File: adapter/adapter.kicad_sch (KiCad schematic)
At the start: 32 parts, among them J1 Serial, J10 Ribbon, J11 Ribbon, J12 Ribbon, J13 serial, J14 serial, J2 Serial, J3 battery charge, J4 RGB, J5 RGB, J6 battery charge, J7 trackball, J8 trackball, J9 Ribbon, SW1 SW_SPST, SW2 SW_SPST, SW3 SW_SPDT, SW4 SW_SPDT, U1 eliteC, U2 eliteC

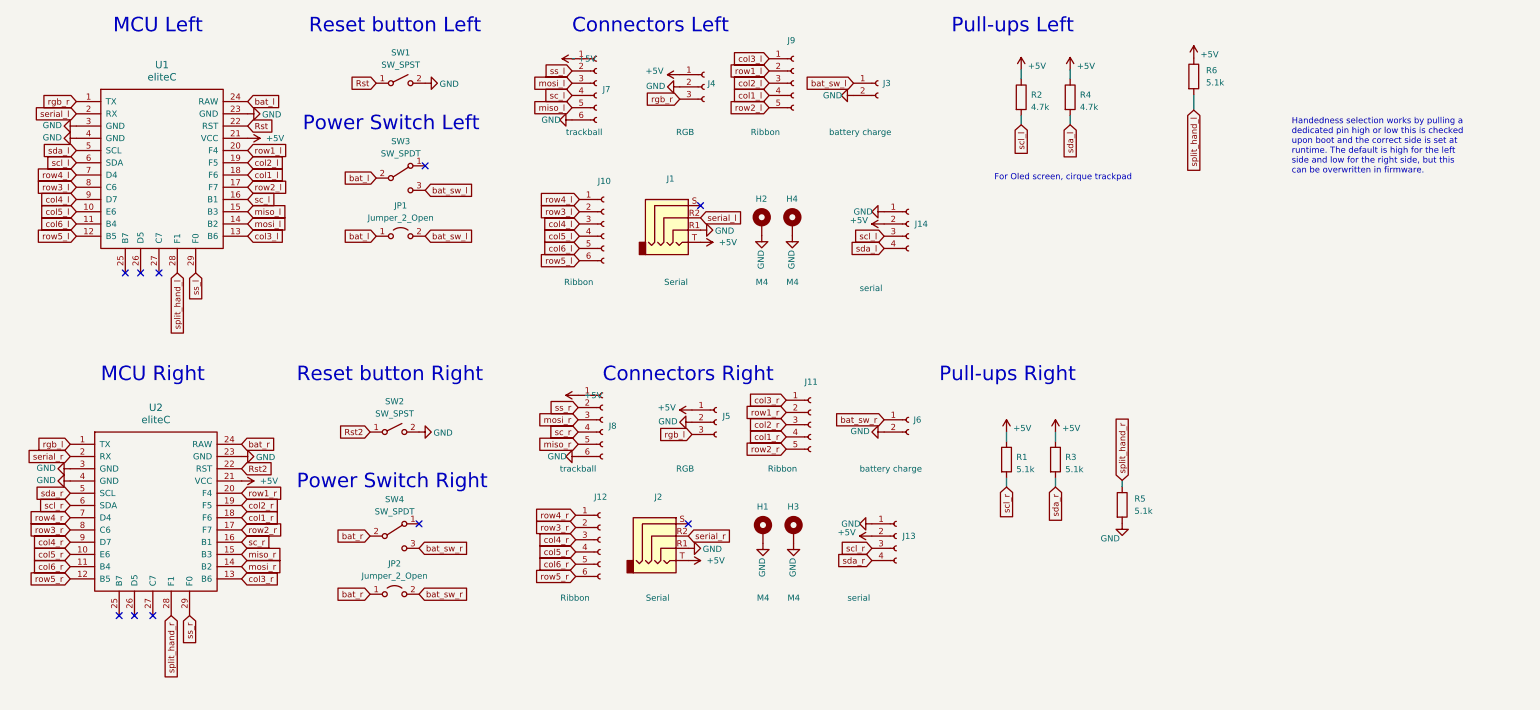
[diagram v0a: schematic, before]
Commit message: updated schematic
- updated schematic to reflect pcb changes
- removed rgb, serial, swapped spi pinout, updated battery footprint
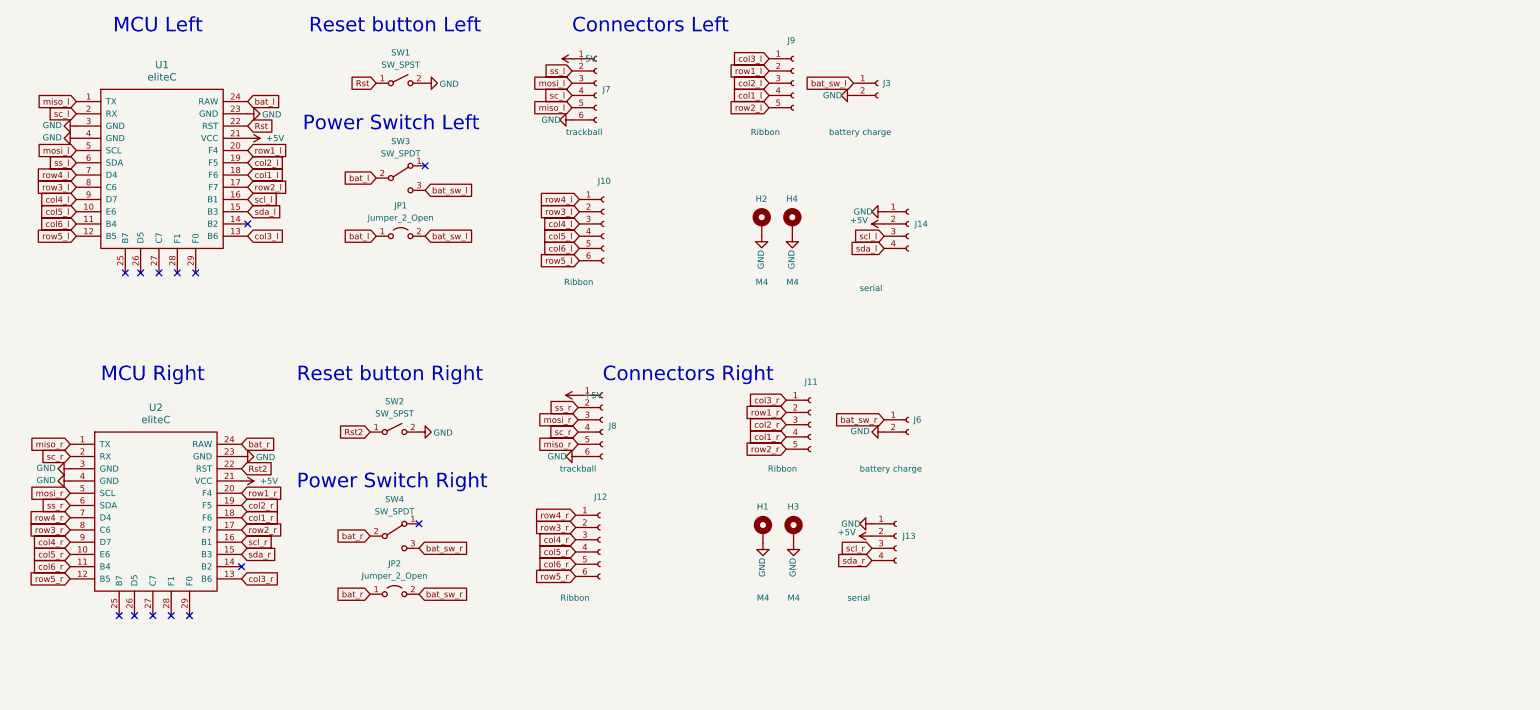
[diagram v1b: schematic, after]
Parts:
- removed J1, J2: Serial, Library:Jack_3.5mm_PJ320E_Horizontal, symbol Connector:AudioJack4
- removed J4, J5: RGB, Library:header1x03, symbol Connector:Conn_01x03_Female
- removed R1, R3, R5, R6: 5.1k, Library:R_1206_handsolder, symbol Device:R
- removed R2, R4: 4.7k, Library:R_1206_handsolder, symbol Device:R
- J3, J6: footprint Library:PinHeader_1x02_P2.54mm_Vertical -> Connector_JST:JST_PH_B2B-PH-K_1x02_P2.00mm_Vertical
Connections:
- net rgb_l is gone; now on net miso_r: U2.1 (TX)
- net rgb_r is gone; now on net miso_l: U1.1 (TX)
- net serial_l is gone; now on net sc_l: U1.2 (RX)
- net serial_r is gone; now on net sc_r: U2.2 (RX)
- net miso_l: no longer U1.15 (B3)
- net miso_r: no longer U2.15 (B3)
- net mosi_l: now also U1.5 (SCL); no longer U1.14 (B2)
- net mosi_r: now also U2.5 (SCL); no longer U2.14 (B2)
- net sc_l: no longer U1.16 (B1)
- net sc_r: no longer U2.16 (B1)
- net scl_l: now also U1.16 (B1); no longer U1.6 (SDA)
- net scl_r: now also U2.16 (B1); no longer U2.6 (SDA)
- net sda_l: now also U1.15 (B3); no longer U1.5 (SCL)
- net sda_r: now also U2.15 (B3); no longer U2.5 (SCL)
- net ss_l: now also U1.6 (SDA); no longer U1.29 (F0)
- net ss_r: now also U2.6 (SDA); no longer U2.29 (F0)
- net split_hand_l: no longer names the net of U1.28 (F1)
- net split_hand_r: no longer names the net of U2.28 (F1)
- no-connect marks 10 -> 14
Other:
- note removed: "For Oled screen, cirque trackpad"
- note removed: "Handedness selection works by pulling a dedicated pin high or low this is checked upon boot and the correct side is set at runtime. The default is high for the left side and low for the right side, but this can be overwritten in firmware."
- note removed: "Pull-ups Left"
- note removed: "Pull-ups Right"
